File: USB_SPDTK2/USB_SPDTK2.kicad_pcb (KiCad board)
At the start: 2 copper layers, 34 x 50 mm, 65 parts, among them J1 USB_B_Micro, J2 TagConnectTC2050, J3 Conn_02x08_Odd_Even, SW1 SW_Push, SW2 SW_Push, U1 LM27313XMF, U2 LP2985-3.3, U4 STM32F411RETx, U5 93LC66AT-IOT, U6 L293DD, Y1 16M 20pF 3225

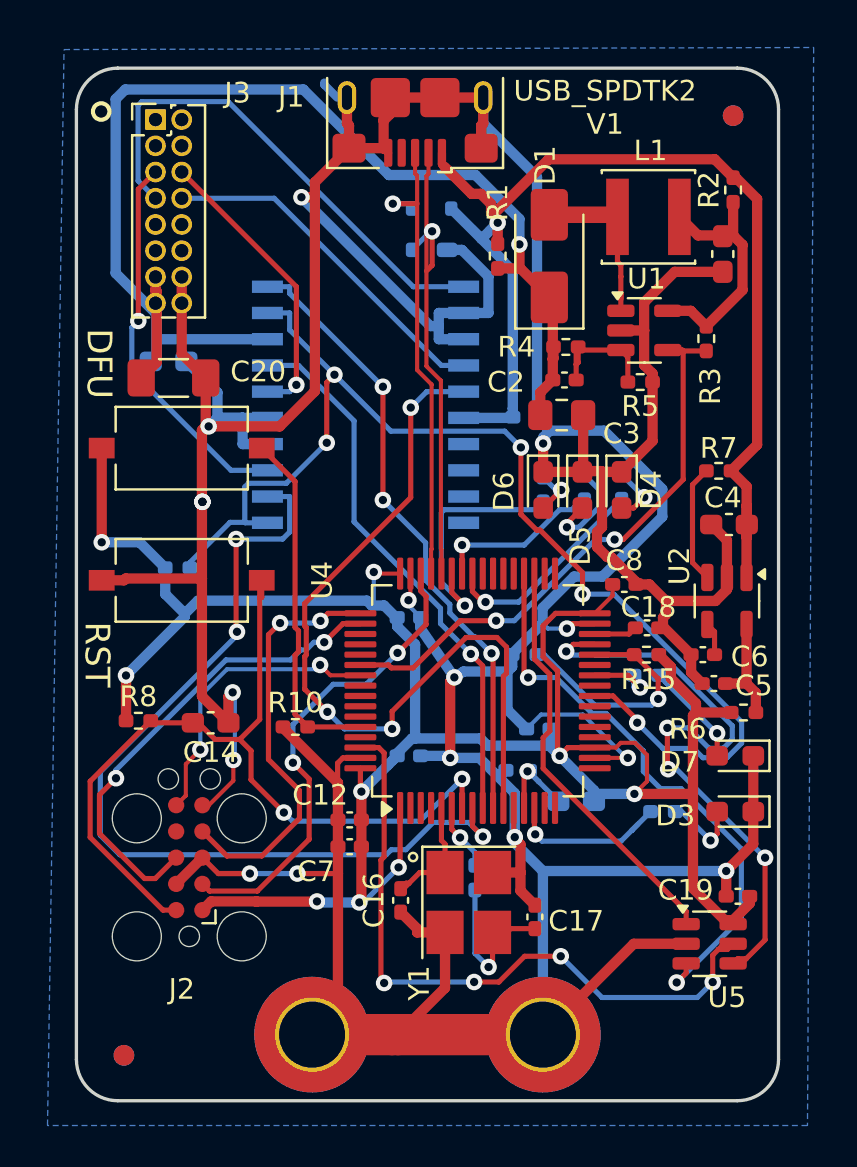
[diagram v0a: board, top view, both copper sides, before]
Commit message: Update to v1.1, fix incorrect footprint for L293DD
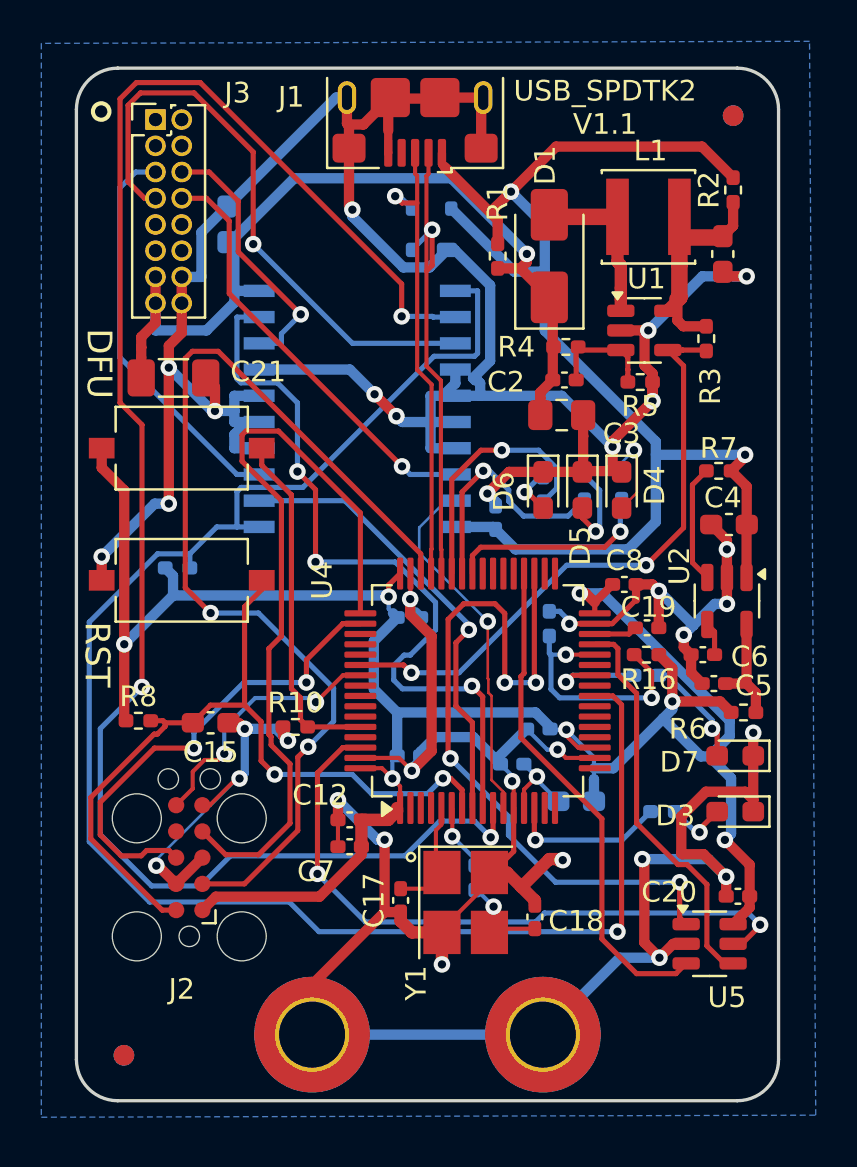
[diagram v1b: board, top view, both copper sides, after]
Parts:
- removed U6: L293DD, Package_SO:SO-20_12.8x7.5mm_P1.27mm
- added U3: L293DD, Package_SO:SO-20_12.8x7.5mm_P1.27mm, B.Cu at (121.2, 80.2)
- moved C14 7.22 mm to (114.9, 71.3), turned to -90 degrees
- moved C16 5.06 mm to (127.9, 85.5), turned to -90 degrees
- moved R18 1.92 mm to (130.5, 90.6), turned to 90 degrees
- moved C13 0.40 mm to (128.7, 97.4)
- moved Y1 0.15 mm to (126.5, 104.1)
- renumbered C15 to C14, C14 to C15, C21 to C16, C16 to C17, C17 to C18, C18 to C19, C19 to C20, C20 to C21, R18 to R12, R12 to R13, R13 to R14, R14 to R15, R15 to R16, R16 to R17, R17 to R18
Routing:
- net S2U: track 30.4 -> 82.1 mm
- net GND: track 299.9 -> 267.1 mm, vias 16 -> 33
- net /Controller/JTMS: track 23.3 -> 50.2 mm
- net SW_Enable: track 58.7 -> 81.6 mm, vias 5 -> 1
- net S2D: track 39.7 -> 17.1 mm, vias 3 -> 1
- net S1U: track 44.1 -> 22.1 mm, vias 3 -> 1
- net +VSW: track 59.9 -> 41.2 mm
- net /Controller/JTCK: track 20.3 -> 37.9 mm, vias 2 -> 0
- net /Controller/SPI2_MISO: track 20.3 -> 36.5 mm, vias 0 -> 4
- net /Controller/SPI2_SCK: track 30.2 -> 18.8 mm, vias 4 -> 0
- net S1D: track 26.6 -> 37.1 mm, vias 1 -> 3
- net VBUS: track 56.2 -> 65.5 mm, vias 1 -> 2
- net S2U_OUT: track 24.4 -> 29.1 mm, vias 0 -> 1
- net /Controller/SPI2_MOSI: track 28.3 -> 24.4 mm, vias 2 -> 0
- net S2D_OUT: track 17.0 -> 20.8 mm, vias 0 -> 1
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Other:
- board text added: "USB_SPDTK2 V1.1"
- board text removed: "USB_SPDTK2 V1"

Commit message: Fix connector and C21 interference.
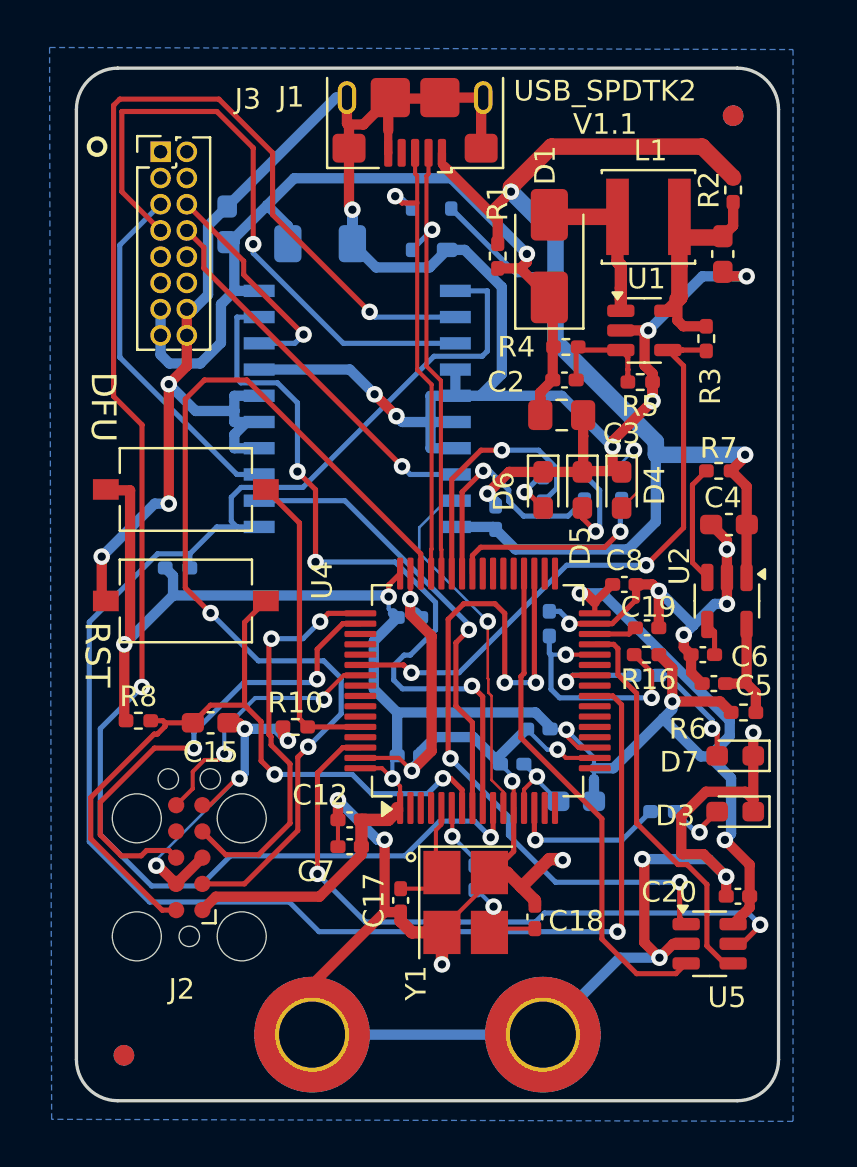
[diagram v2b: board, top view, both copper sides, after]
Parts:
- C21: moved to B.Cu
- moved C21 9.63 mm to (119.4, 72.2)
- moved SW2 2.01 mm to (112.9, 84.1)
- moved J3 1.58 mm to (111.7, 67.8)
- moved SW1 1.02 mm to (112.9, 89.5)
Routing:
- net /Controller/JTCK: track 37.9 -> 19.6 mm, vias 0 -> 2
- net S2D_OUT: track 20.8 -> 18.5 mm
- net Net-(U4-BOOT0): track 17.0 -> 14.9 mm
- net S1U_OUT: track 19.4 -> 17.3 mm
- net S1D_OUT: track 12.9 -> 11.0 mm
- net /Controller/USB-: track 24.2 -> 22.5 mm
- net /Controller/JTMS: track 50.2 -> 48.7 mm
- net VBUS: track 65.5 -> 66.8 mm
- net +3.3V: track 109.3 -> 108.1 mm
- net S2U_OUT: track 29.1 -> 30.3 mm
- net SW_Enable: track 81.6 -> 82.7 mm
- net Net-(J2-~{RESET}): track 38.9 -> 38.0 mm
- net GND: track 267.1 -> 268.0 mm, vias 33 -> 32
